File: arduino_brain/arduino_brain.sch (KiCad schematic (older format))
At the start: 40 parts

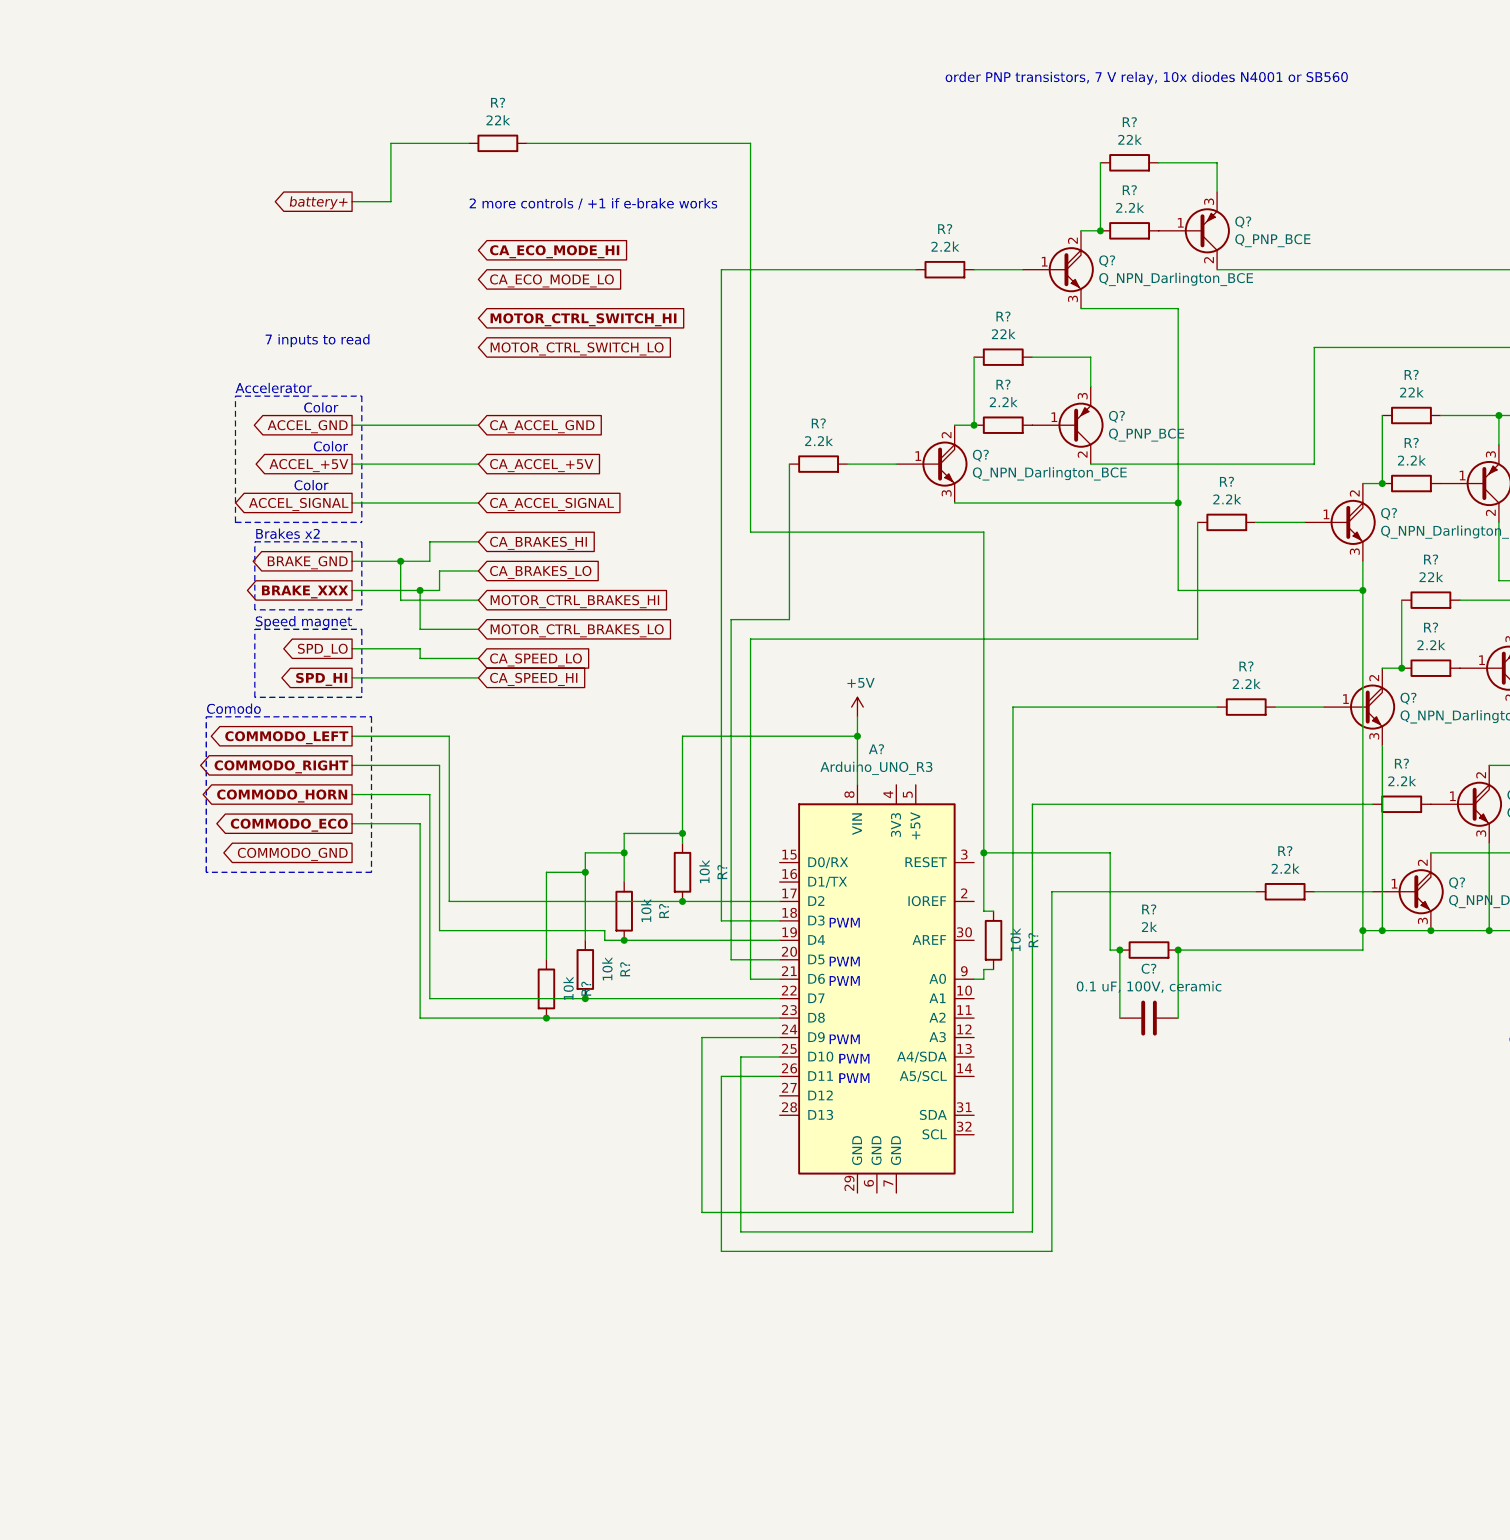
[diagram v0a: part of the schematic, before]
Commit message: Added 5V regulator to schematic
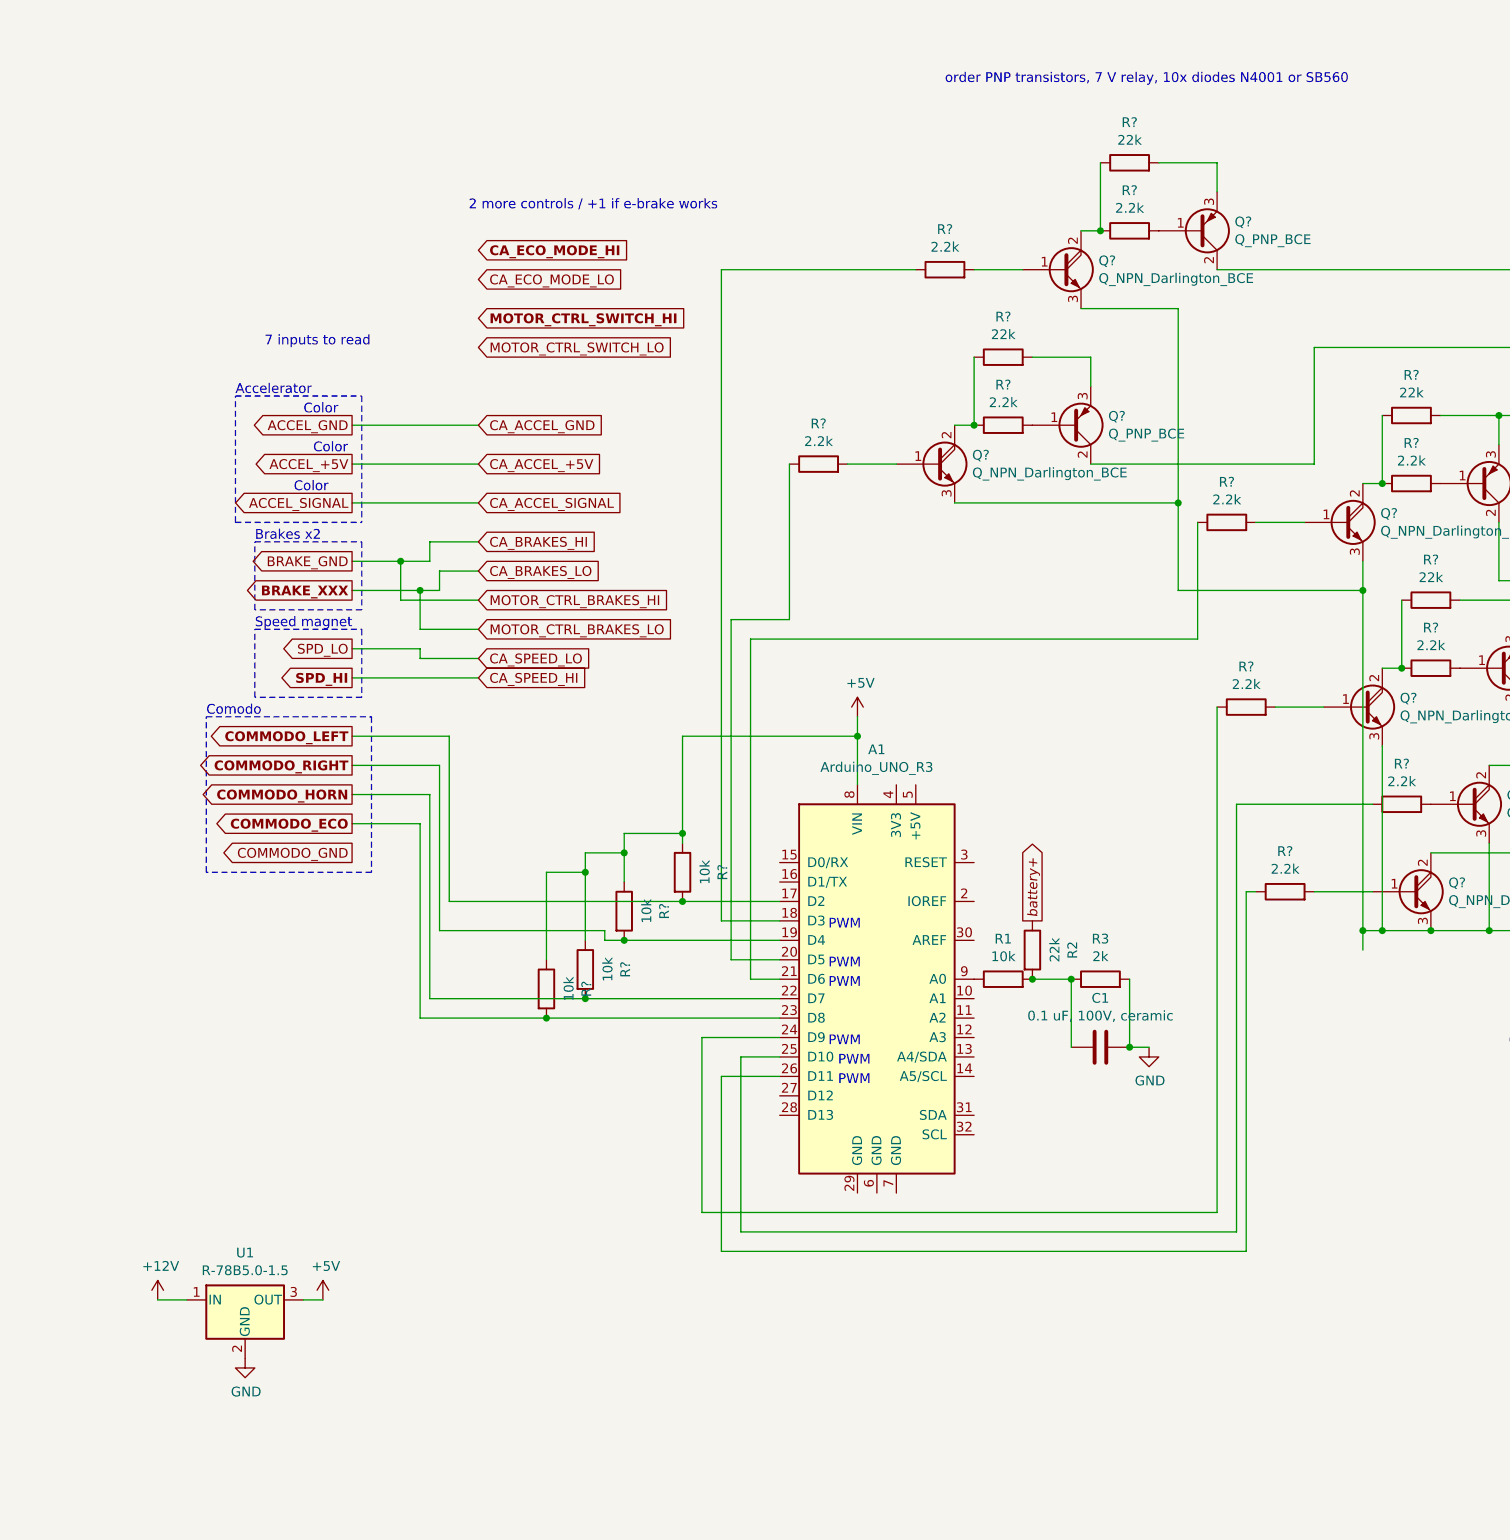
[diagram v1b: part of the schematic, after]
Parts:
- added U1: R-78B5.0-1.5, Converter_DCDC:Converter_DCDC_RECOM_R-78B-2.0_THT, symbol Regulator_Switching:R-78B5.0-2.0
- gave numbers to parts that had none: 5
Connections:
- net +12V: now also U1.1 (IN)
- net +5V: now also U1.3 (OUT)
- net GND: now also U1.2 (GND)
- net at C1.1, R2.2, R3.1: now also R1.2; no longer R1.1
- net at A1.9 (A0): now also R1.1; no longer R1.2
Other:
- moved on the sheet: C1, R1, R2, R3
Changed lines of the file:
@@
 Text Notes 4700 900  0    50   ~ 0
 order PNP transistors, 7 V relay, 10x diodes N4001 or SB560
-Text GLabel 1650 1500 0    50   Output Italic 0
-battery+
 Text Notes 7600 5850 0    50   ~ 0
 6 lights/things to control
@@
 ~
 $Comp
-L MCU_Module:Arduino_UNO_R3 A?
+L MCU_Module:Arduino_UNO_R3 A1
 U 1 1 5E167047
 P 4350 5500
-F 0 "A?" H 4350 6681 50  0000 C CNN
+F 0 "A1" H 4350 6681 50  0000 C CNN
 F 1 "Arduino_UNO_R3" H 4350 6590 50  0000 C CNN
 F 2 "Module:Arduino_UNO_R3" H 4500 4450 50  0001 L CNN
@@
 Connection ~ 2650 5700
 Wire Wire Line
-	6300 5050 5250 5050
-Wire Wire Line
-	5250 5050 5250 6900
-Wire Wire Line
-	5250 6900 3550 6900
-Wire Wire Line
 	3550 6900 3550 6000
 Wire Wire Line
 	3550 6000 3850 6000
 Wire Wire Line
-	6900 4600 5150 4600
-Wire Wire Line
-	5150 4600 5150 6800
-Wire Wire Line
-	5150 6800 3650 6800
-Wire Wire Line
 	3650 6800 3650 5900
 Wire Wire Line
 	3650 5900 3850 5900
 Wire Wire Line
-	6100 4100 5050 4100
-Wire Wire Line
-	5050 4100 5050 6700
-Wire Wire Line
-	5050 6700 3450 6700
-Wire Wire Line
 	3450 6700 3450 5800
 Wire Wire Line
@@
 Wire Wire Line
 	3550 5200 3850 5200
-$Comp
-L Device:R R?
-U 1 1 5E0F06FF
-P 2400 1200
-F 0 "R?" V 2607 1200 50  0000 C CNN
-F 1 "22k" V 2516 1200 50  0000 C CNN
-F 2 "" V 2330 1200 50  0001 C CNN
-F 3 "~" H 2400 1200 50  0001 C CNN
-	1    2400 1200
-	0    -1   -1   0
-$EndComp
-Wire Wire Line
-	2250 1200 1850 1200
-Wire Wire Line
-	1850 1200 1850 1500
-Wire Wire Line
-	1850 1500 1650 1500
-Wire Wire Line
-	4850 5500 4900 5500
-Wire Wire Line
-	4900 5500 4900 5450
-Wire Wire Line
-	4900 3200 3700 3200
-Wire Wire Line
-	3700 3200 3700 1200
-Wire Wire Line
-	3700 1200 2550 1200
-$Comp
-L Device:R R?
-U 1 1 5E10520B
-P 4950 5300
-F 0 "R?" V 5157 5300 50  0000 C CNN
-F 1 "10k" V 5066 5300 50  0000 C CNN
-F 2 "" V 4880 5300 50  0001 C CNN
-F 3 "~" H 4950 5300 50  0001 C CNN
-	1    4950 5300
-	1    0    0    -1
-$EndComp
-Wire Wire Line
-	4950 5150 4900 5150
-Wire Wire Line
-	4900 5150 4900 4850
-Wire Wire Line
-	4950 5450 4900 5450
-$Comp
-L Device:R R?
-U 1 1 5E11941E
-P 5750 5350
-F 0 "R?" V 5957 5350 50  0000 C CNN
-F 1 "2k" V 5866 5350 50  0000 C CNN
-F 2 "" V 5680 5350 50  0001 C CNN
-F 3 "~" H 5750 5350 50  0001 C CNN
-	1    5750 5350
-	0    -1   -1   0
-$EndComp
-Wire Wire Line
-	5600 5350 5550 5350
-Wire Wire Line
-	5550 5350 5550 4850
-Wire Wire Line
-	5550 4850 4900 4850
-Connection ~ 4900 4850
-Wire Wire Line
-	4900 4850 4900 3200
-Wire Wire Line
-	5900 5350 6850 5350
 Wire Wire Line
 	6850 5350 6850 5250
 Connection ~ 6850 5250
 $Comp
-L Device:C C?
+L Regulator_Switching:R-78B5.0-2.0 U1
+U 1 1 5E105FCA
+P 1100 7150
+F 0 "U1" H 1100 7392 50  0000 C CNN
+F 1 "R-78B5.0-1.5" H 1100 7301 50  0000 C CNN
+F 2 "Converter_DCDC:Converter_DCDC_RECOM_R-78B-2.0_THT" H 1150 6900 50  0001 L CIN
+F 3 "https://www.recom-power.com/pdf/Innoline/R-78Bxx-2.0.pdf" H 1100 7150 50  0001 C CNN
+	1    1100 7150
+	1    0    0    -1
+$EndComp
+$Comp
+L power:+5V #PWR?
+U 1 1 5E107402
+P 1500 7150
+F 0 "#PWR?" H 1500 7000 50  0001 C CNN
+F 1 "+5V" H 1515 7323 50  0000 C CNN
+F 2 "" H 1500 7150 50  0001 C CNN
+F 3 "" H 1500 7150 50  0001 C CNN
+	1    1500 7150
+	1    0    0    -1
+$EndComp
+$Comp
+L power:+12V #PWR?
+U 1 1 5E107F0F
+P 650 7150
+F 0 "#PWR?" H 650 7000 50  0001 C CNN
+F 1 "+12V" H 665 7323 50  0000 C CNN
+F 2 "" H 650 7150 50  0001 C CNN
+F 3 "" H 650 7150 50  0001 C CNN
+	1    650  7150
+	1    0    0    -1
+$EndComp
+$Comp
+L power:GND #PWR?
+U 1 1 5E108737
+P 1100 7450
+F 0 "#PWR?" H 1100 7200 50  0001 C CNN
+F 1 "GND" H 1105 7277 50  0000 C CNN
+F 2 "" H 1100 7450 50  0001 C CNN
+F 3 "" H 1100 7450 50  0001 C CNN
+	1    1100 7450
+	1    0    0    -1
+$EndComp
+Connection ~ 5350 5500
+$Comp
+L Device:R R3
+U 1 1 5E11941E
+P 5500 5500
+F 0 "R3" V 5707 5500 50  0000 C CNN
+F 1 "2k" V 5616 5500 50  0000 C CNN
+F 2 "" V 5430 5500 50  0001 C CNN
+F 3 "~" H 5500 5500 50  0001 C CNN
+	1    5500 5500
+	0    -1   -1   0
+$EndComp
+Wire Wire Line
+	5650 5850 5650 5500
+Wire Wire Line
+	5350 5850 5350 5500
+$Comp
+L Device:C C1
 U 1 1 5E12E82D
-P 5750 5700
-F 0 "C?" V 6002 5700 50  0000 C CNN
-F 1 "0.1 uF, 100V, ceramic" V 5911 5700 50  0000 C CNN
-F 2 "" H 5788 5550 50  0001 C CNN
-F 3 "~" H 5750 5700 50  0001 C CNN
-	1    5750 5700
-	0    -1   -1   0
-$EndComp
-Wire Wire Line
-	5600 5700 5600 5350
-Connection ~ 5600 5350
-Wire Wire Line
-	5900 5700 5900 5350
-Connection ~ 5900 5350
+P 5500 5850
+F 0 "C1" V 5752 5850 50  0000 C CNN
+F 1 "0.1 uF, 100V, ceramic" V 5661 5850 50  0000 C CNN
+F 2 "" H 5538 5700 50  0001 C CNN
+F 3 "~" H 5500 5850 50  0001 C CNN
+	1    5500 5850
+	0    -1   -1   0
+$EndComp
+Wire Wire Line
+	6200 6800 3650 6800
+Wire Wire Line
+	6900 4600 6200 4600
+Wire Wire Line
+	6200 4600 6200 6800
+Wire Wire Line
+	6100 6700 3450 6700
+Wire Wire Line
+	6100 4100 6100 6700
+Wire Wire Line
+	6250 6900 3550 6900
+Wire Wire Line
+	6300 5050 6250 5050
+Wire Wire Line
+	6250 5050 6250 6900
+$Comp
+L Device:R R1
+U 1 1 5E10520B
+P 5000 5500
+F 0 "R1" V 5207 5500 50  0000 C CNN
+F 1 "10k" V 5116 5500 50  0000 C CNN
+F 2 "" V 4930 5500 50  0001 C CNN
+F 3 "~" H 5000 5500 50  0001 C CNN
+	1    5000 5500
+	0    -1   -1   0
+$EndComp
+Text GLabel 5150 5200 1    50   Output Italic 0
+battery+
+Connection ~ 5150 5500
+Wire Wire Line
+	5150 5500 5350 5500
+$Comp
+L Device:R R2
+U 1 1 5E0F06FF
+P 5150 5350
+F 0 "R2" V 5357 5350 50  0000 C CNN
+F 1 "22k" V 5266 5350 50  0000 C CNN
+F 2 "" V 5080 5350 50  0001 C CNN
+F 3 "~" H 5150 5350 50  0001 C CNN
+	1    5150 5350
+	1    0    0    -1
+$EndComp
+Wire Wire Line
+	1400 7150 1500 7150
+Wire Wire Line
+	800  7150 650  7150
+$Comp
+L power:GND #PWR?
+U 1 1 5E27DA33
+P 5750 5850
+F 0 "#PWR?" H 5750 5600 50  0001 C CNN
+F 1 "GND" H 5755 5677 50  0000 C CNN
+F 2 "" H 5750 5850 50  0001 C CNN
+F 3 "" H 5750 5850 50  0001 C CNN
+	1    5750 5850
+	1    0    0    -1
+$EndComp
+Wire Wire Line
+	5650 5850 5750 5850
+Connection ~ 5650 5850
 $EndSCHEMATC

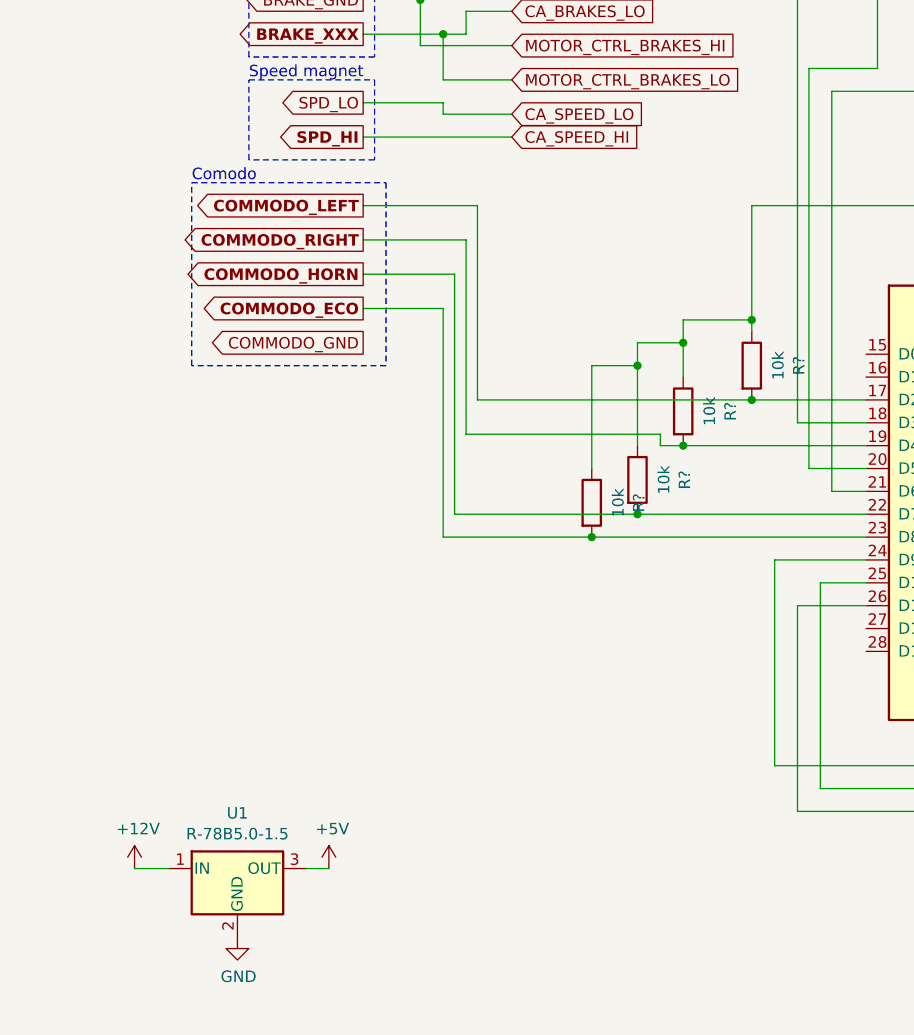
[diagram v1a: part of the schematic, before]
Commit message: Added diode to 5V regulator
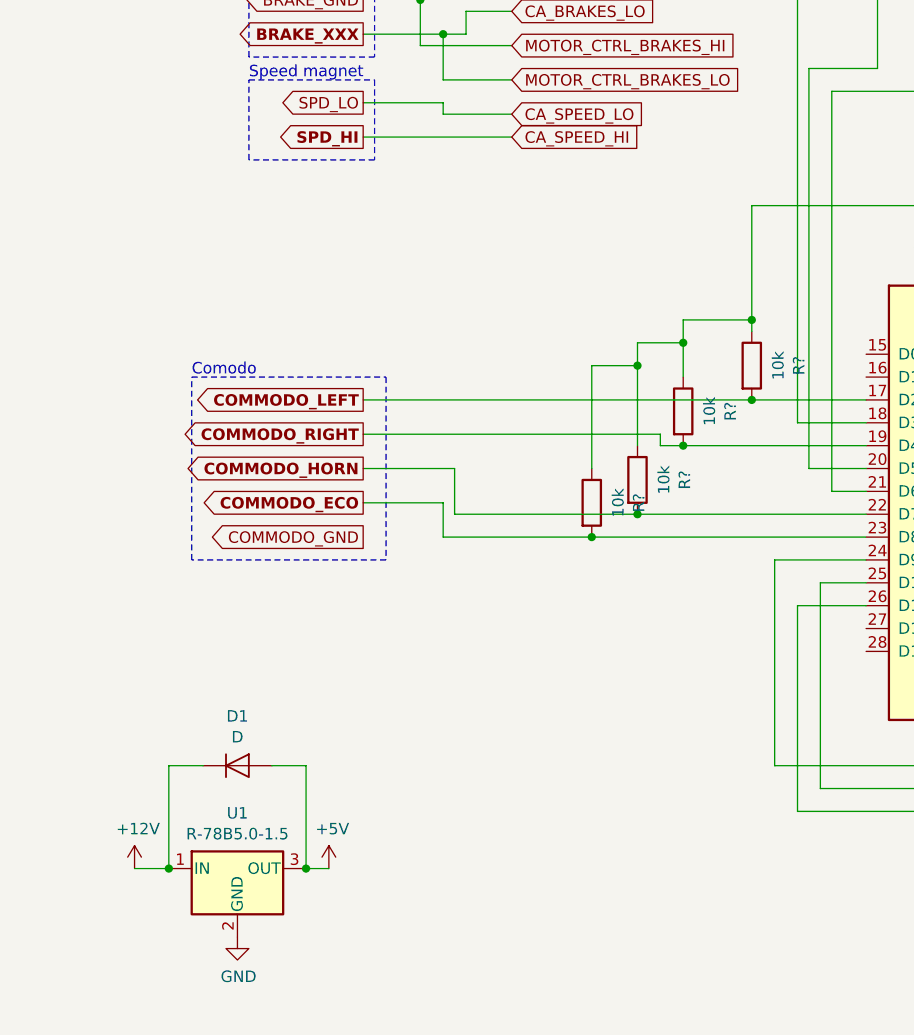
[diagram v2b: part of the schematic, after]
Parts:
- added D1: D, symbol Device:D
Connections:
- net +12V: now also D1.1 (K)
- net +5V: now also D1.2 (A)
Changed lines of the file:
@@
 Text Notes 1150 3700 0    50   ~ 0
 Speed magnet
-Text GLabel 1650 4250 0    50   Output ~ 10
+Text GLabel 1650 5100 0    50   Output ~ 10
 COMMODO_LEFT
-Text GLabel 1650 4400 0    50   Output ~ 10
+Text GLabel 1650 5250 0    50   Output ~ 10
 COMMODO_RIGHT
-Text GLabel 1650 4550 0    50   Output ~ 10
+Text GLabel 1650 5400 0    50   Output ~ 10
 COMMODO_HORN
-Text GLabel 1650 4700 0    50   Output ~ 10
+Text GLabel 1650 5550 0    50   Output ~ 10
 COMMODO_ECO
-Text GLabel 1650 4850 0    50   Output ~ 0
+Text GLabel 1650 5700 0    50   Output ~ 0
 COMMODO_GND
 Text Notes -1100 5050 0    50   ~ 0
@@
 $EndComp
 Wire Notes Line
-	1750 4950 900  4950
+	1750 5800 900  5800
 Wire Notes Line
-	900  4950 900  4150
+	900  5800 900  5000
 Wire Notes Line
-	900  4150 1750 4150
+	900  5000 1750 5000
 Wire Notes Line
-	1750 4150 1750 4950
-Text Notes 900  4150 0    50   ~ 0
+	1750 5000 1750 5800
+Text Notes 900  5000 0    50   ~ 0
 Comodo
 $Comp
@@
 Wire Wire Line
 	3350 5100 3850 5100
-Wire Wire Line
-	2150 5100 2150 4250
-Wire Wire Line
-	2150 4250 1650 4250
 $Comp
 L Device:R R?
@@
 $EndComp
 Wire Wire Line
-	2100 4400 1650 4400
-Wire Wire Line
 	3050 5000 3050 4850
 Wire Wire Line
@@
 $EndComp
 Wire Wire Line
-	2050 4550 1650 4550
+	2050 5400 1650 5400
 Wire Wire Line
 	2850 5300 2850 4950
@@
 $EndComp
 Wire Wire Line
-	2000 4700 1650 4700
+	2000 5550 1650 5550
 Wire Wire Line
 	2650 5400 2650 4950
@@
 PWM
 Wire Wire Line
-	2150 5100 3350 5100
-Wire Wire Line
 	3050 5300 3850 5300
 Wire Wire Line
@@
 Wire Wire Line
 	2950 5300 2950 5250
-Wire Wire Line
-	2950 5250 2100 5250
-Wire Wire Line
-	2100 4400 2100 5250
 Connection ~ 3050 5300
 Wire Wire Line
@@
 Wire Wire Line
 	2850 5600 2050 5600
-Wire Wire Line
-	2050 4550 2050 5600
 Connection ~ 2850 5600
 Wire Wire Line
@@
 Wire Wire Line
 	2650 5700 2000 5700
-Wire Wire Line
-	2000 4700 2000 5700
 Connection ~ 2650 5700
 Wire Wire Line
@@
 	5650 5850 5750 5850
 Connection ~ 5650 5850
+Wire Wire Line
+	2000 5550 2000 5700
+Wire Wire Line
+	2050 5400 2050 5600
+Wire Wire Line
+	1650 5250 2950 5250
+Wire Wire Line
+	1650 5100 3350 5100
+$Comp
+L Device:D D1
+U 1 1 5E291EAE
+P 1100 6700
+F 0 "D1" H 1100 6916 50  0000 C CNN
+F 1 "D" H 1100 6825 50  0000 C CNN
+F 2 "" H 1100 6700 50  0001 C CNN
+F 3 "~" H 1100 6700 50  0001 C CNN
+	1    1100 6700
+	1    0    0    -1
+$EndComp
+Wire Wire Line
+	1250 6700 1400 6700
+Wire Wire Line
+	1400 6700 1400 7150
+Connection ~ 1400 7150
+Wire Wire Line
+	950  6700 800  6700
+Wire Wire Line
+	800  6700 800  7150
+Connection ~ 800  7150
 $EndSCHEMATC
